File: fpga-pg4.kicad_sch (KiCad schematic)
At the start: 16 parts, among them U1 XC7A15T-FTG256

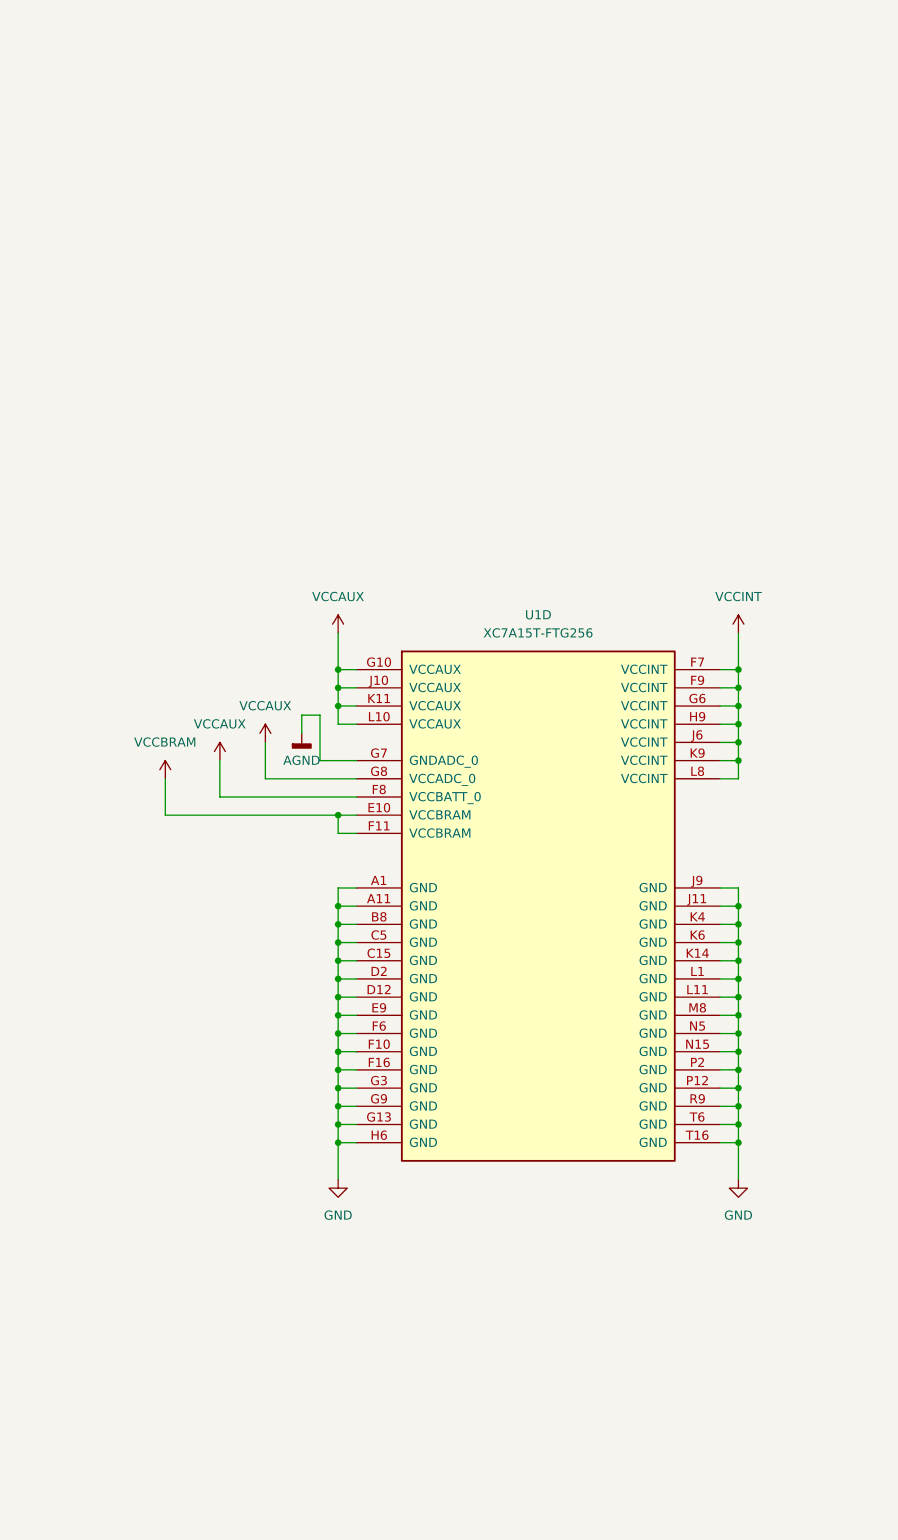
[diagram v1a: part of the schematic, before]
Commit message: changed ftg256 to csg325, wanted xc7a12t but couldnt find
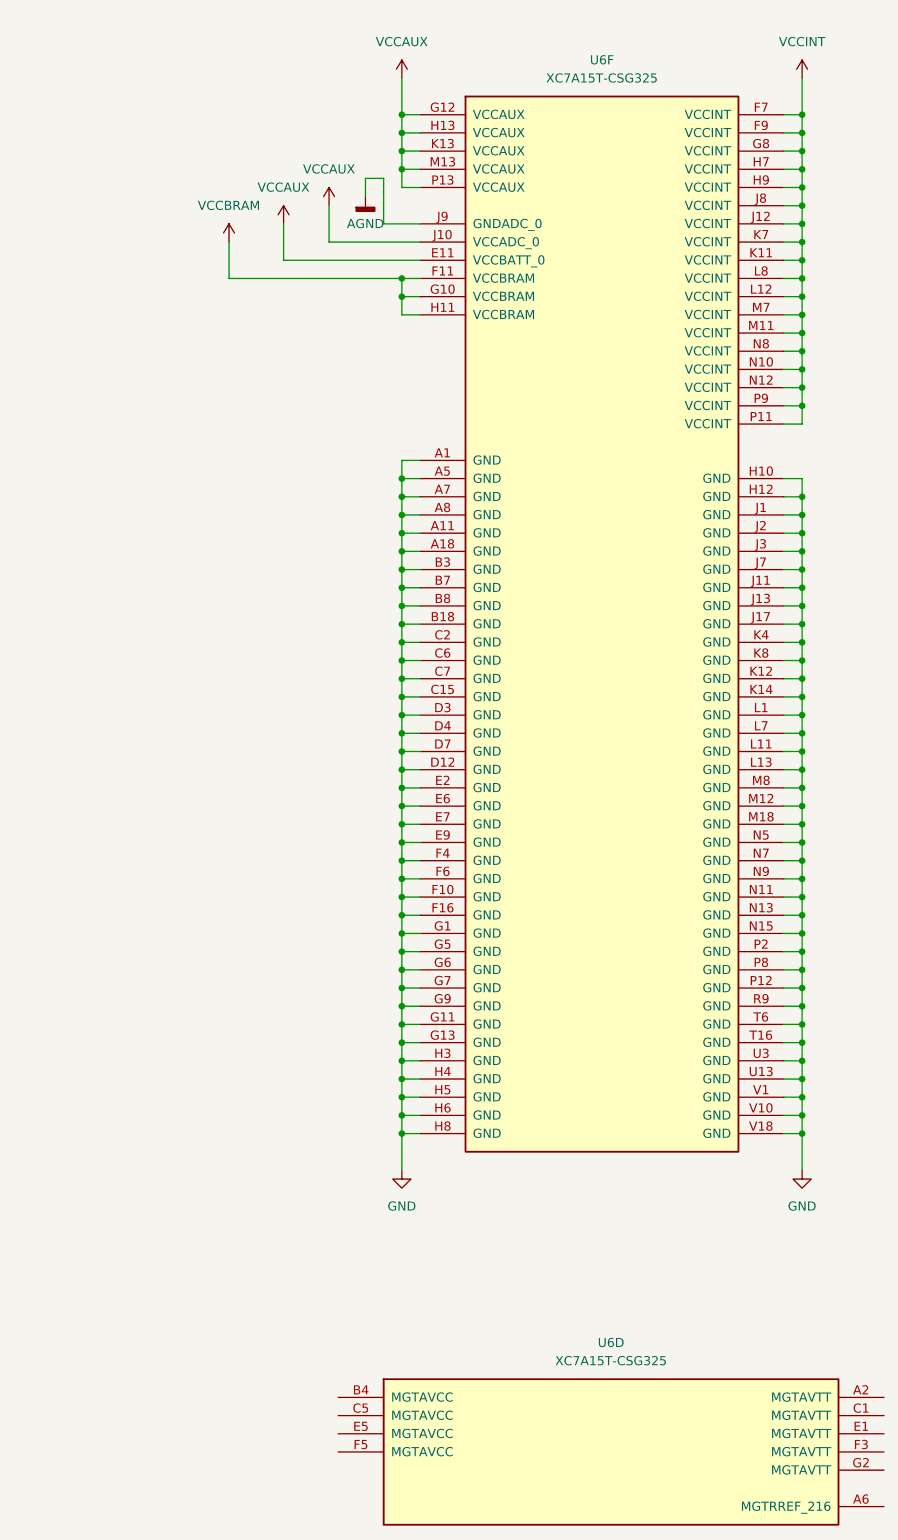
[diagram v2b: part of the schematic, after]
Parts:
- removed U1: XC7A15T-FTG256, Package_BGA:Xilinx_FTG256, symbol FPGA_Xilinx_Artix7:XC7A15T-FTG256
- added U6: XC7A15T-CSG325, Package_BGA:Xilinx_CSG325, symbol FPGA_Xilinx_Artix7:XC7A15T-CSG325
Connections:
- net AGND: now also U6.J9 (GNDADC_0)
- net GND: now also U6.A1 (GND), U6.A11 (GND), U6.A18 (GND), U6.A5 (GND), U6.A7 (GND), U6.A8 (GND), U6.B18 (GND), U6.B3 (GND), U6.B7 (GND), U6.B8 (GND), U6.C15 (GND), U6.C2 (GND), U6.C6 (GND), U6.C7 (GND), U6.D12 (GND), U6.D3 (GND), U6.D4 (GND), U6.D7 (GND), U6.E2 (GND), U6.E6 (GND), U6.E7 (GND), U6.E9 (GND), U6.F10 (GND), U6.F16 (GND), U6.F4 (GND), U6.F6 (GND), U6.G1 (GND), U6.G11 (GND), U6.G13 (GND), U6.G5 (GND), U6.G6 (GND), U6.G7 (GND), U6.G9 (GND), U6.H10 (GND), U6.H12 (GND), U6.H3 (GND), U6.H4 (GND), U6.H5 (GND), U6.H6 (GND), U6.H8 (GND), U6.J1 (GND), U6.J11 (GND), U6.J13 (GND), U6.J17 (GND), U6.J2 (GND), U6.J3 (GND), U6.J7 (GND), U6.K12 (GND), U6.K14 (GND), U6.K4 (GND), U6.K8 (GND), U6.L1 (GND), U6.L11 (GND), U6.L13 (GND), U6.L7 (GND), U6.M12 (GND), U6.M18 (GND), U6.M8 (GND), U6.N11 (GND), U6.N13 (GND), U6.N15 (GND), U6.N5 (GND), U6.N7 (GND), U6.N9 (GND), U6.P12 (GND), U6.P2 (GND), U6.P8 (GND), U6.R9 (GND), U6.T16 (GND), U6.T6 (GND), U6.U13 (GND), U6.U3 (GND), U6.V1 (GND), U6.V10 (GND), U6.V18 (GND)
- net VCCAUX: now also U6.E11 (VCCBATT_0), U6.G12 (VCCAUX), U6.H13 (VCCAUX), U6.J10 (VCCADC_0), U6.K13 (VCCAUX), U6.M13 (VCCAUX), U6.P13 (VCCAUX)
- net VCCBRAM: now also U6.F11 (VCCBRAM), U6.G10 (VCCBRAM), U6.H11 (VCCBRAM)
- net VCCINT: now also U6.F7 (VCCINT), U6.F9 (VCCINT), U6.G8 (VCCINT), U6.H7 (VCCINT), U6.H9 (VCCINT), U6.J12 (VCCINT), U6.J8 (VCCINT), U6.K11 (VCCINT), U6.K7 (VCCINT), U6.L12 (VCCINT), U6.L8 (VCCINT), U6.M11 (VCCINT), U6.M7 (VCCINT), U6.N10 (VCCINT), U6.N12 (VCCINT), U6.N8 (VCCINT), U6.P11 (VCCINT), U6.P9 (VCCINT)

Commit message: working on ddr3
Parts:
- removed unit 4 of U6
- added C30, C35: 4.7u, Capacitor_SMD:C_0805_2012Metric, symbol Device:C
- added C31, C32, C33, C34: 100n, Capacitor_SMD:C_0603_1608Metric, symbol Device:C
- added R17: 100, Capacitor_SMD:C_0402_1005Metric, symbol Device:R
- added U1: XC7A15T-CSG325, Package_BGA:Xilinx_CSG325, symbol FPGA_Xilinx_Artix7:XC7A15T-CSG325
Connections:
- net VCCINT is gone; now on net +V1P0: C10.1, C11.1, C12.1, C13.1, C9.1, U6.F7 (VCCINT), U6.F9 (VCCINT), U6.G8 (VCCINT), U6.H7 (VCCINT), U6.H9 (VCCINT), U6.J12 (VCCINT), U6.J8 (VCCINT), U6.K11 (VCCINT), U6.K7 (VCCINT), U6.L12 (VCCINT), U6.L8 (VCCINT), U6.M11 (VCCINT), U6.M7 (VCCINT), U6.N10 (VCCINT), U6.N12 (VCCINT), U6.N8 (VCCINT), U6.P11 (VCCINT), U6.P9 (VCCINT)
- net GND: now also C30.2, C31.2, C32.2, C33.2, C34.2, C35.2
- net VCCAUX renamed +V1P8
- net VCCBRAM renamed +V1P0
- net +V1P0: now also C30.1, C31.1, C32.1, U1.B4 (MGTAVCC), U1.C5 (MGTAVCC), U1.E5 (MGTAVCC), U1.F5 (MGTAVCC)
- new net: R17.2, U1.A6 (MGTRREF_216)
- new net +V1P2: C33.1, C34.1, C35.1, R17.1, U1.A2 (MGTAVTT), U1.C1 (MGTAVTT), U1.E1 (MGTAVTT), U1.F3 (MGTAVTT), U1.G2 (MGTAVTT)
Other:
- moved on the sheet: C1, C10, C11, C12, C13, C2, C3, C4, C5, C6, C7, C8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

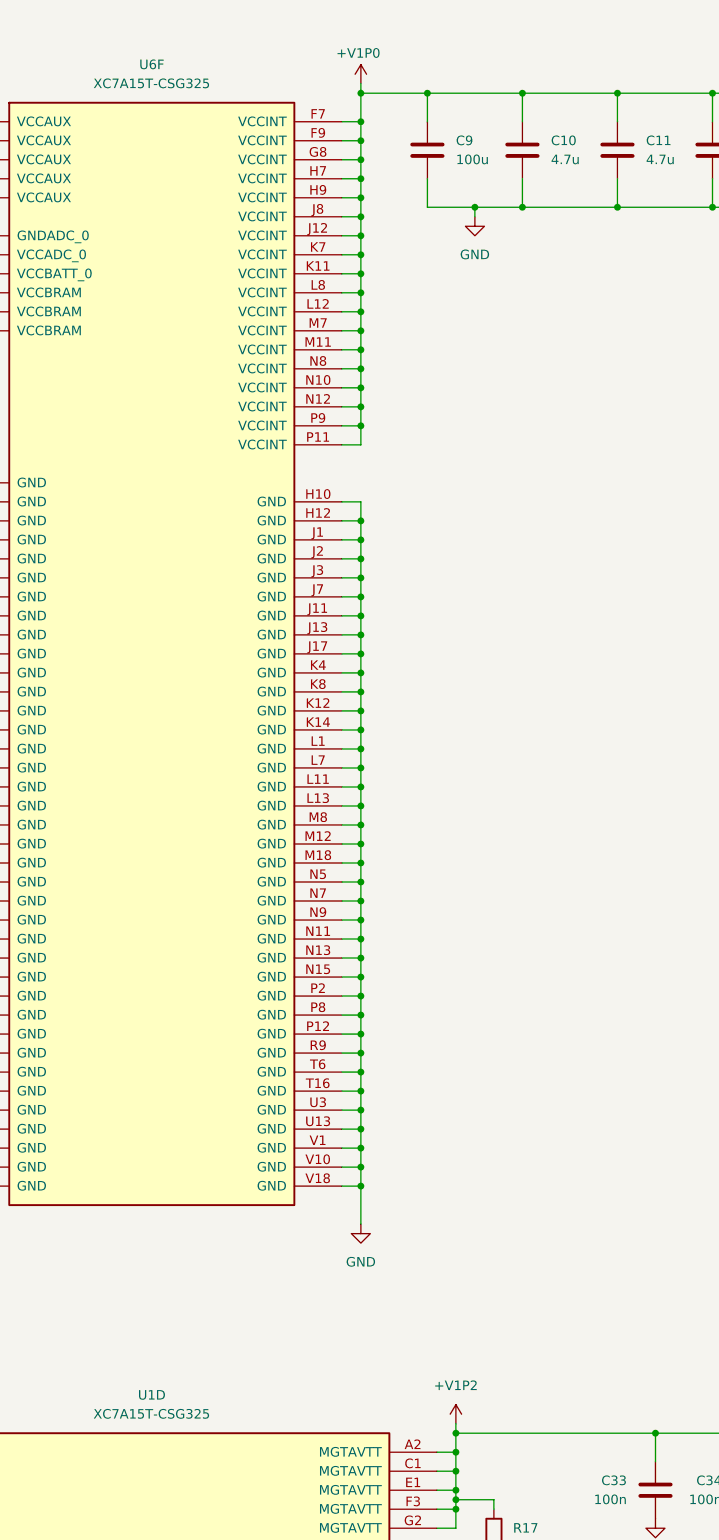
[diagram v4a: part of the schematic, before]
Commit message: placed decoupling caps for fpga
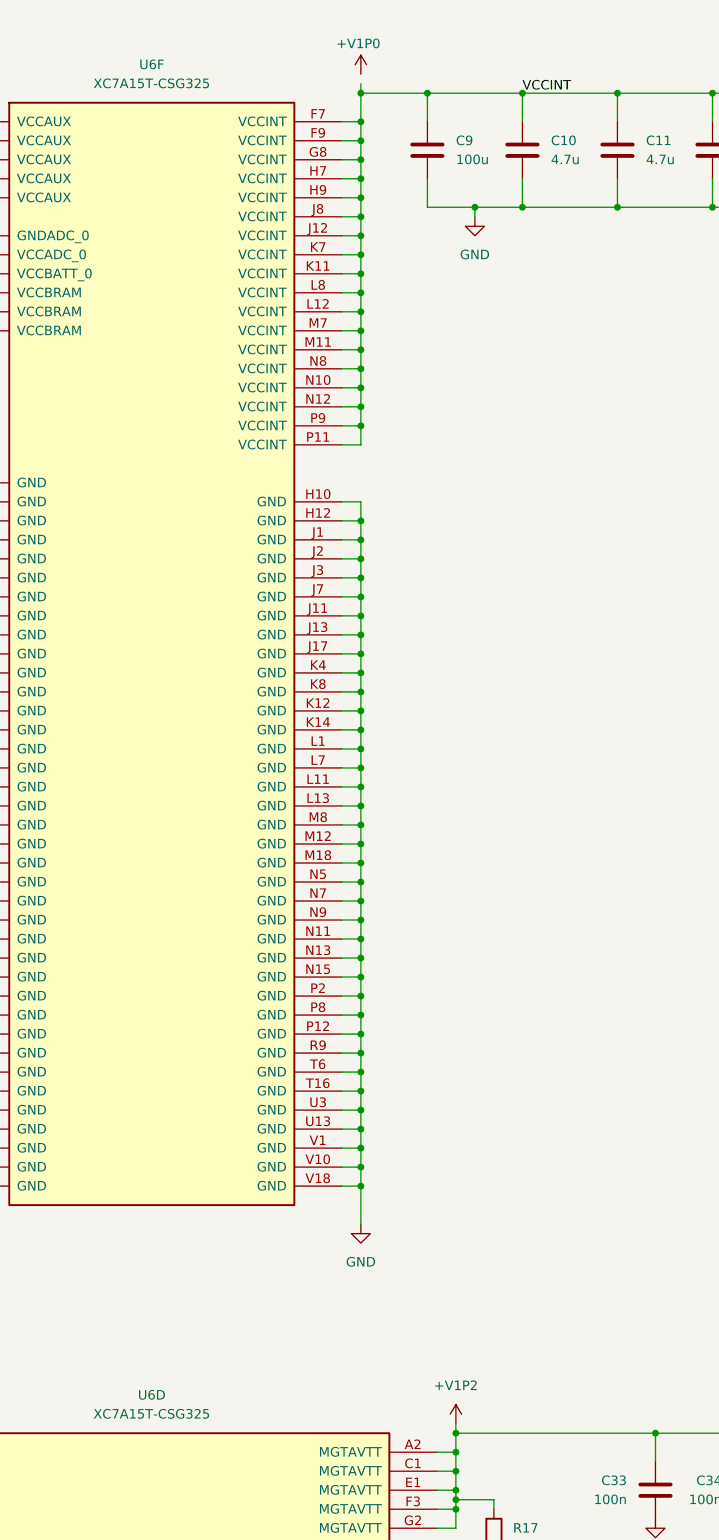
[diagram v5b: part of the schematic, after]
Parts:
- C1, C12, C13, C14, C15, C2, C3, C31, C32, C33, C34, C8: footprint Capacitor_SMD:C_0603_1608Metric -> Capacitor_SMD:C_0402_1005Metric
- C10, C11, C30, C35, C4, C5: footprint Capacitor_SMD:C_0805_2012Metric -> Capacitor_SMD:C_0402_1005Metric
- renumbered U1 to U6
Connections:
- net +V1P0: no longer C10.1, C11.1, C12.1, C13.1, C9.1, U6.F7 (VCCINT), U6.F9 (VCCINT), U6.G8 (VCCINT), U6.H7 (VCCINT), U6.H9 (VCCINT), U6.J12 (VCCINT), U6.J8 (VCCINT), U6.K11 (VCCINT), U6.K7 (VCCINT), U6.L12 (VCCINT), U6.L8 (VCCINT), U6.M11 (VCCINT), U6.M7 (VCCINT), U6.N10 (VCCINT), U6.N12 (VCCINT), U6.N8 (VCCINT), U6.P11 (VCCINT), U6.P9 (VCCINT)
- new net VCCINT: C10.1, C11.1, C12.1, C13.1, C9.1, U6.F7 (VCCINT), U6.F9 (VCCINT), U6.G8 (VCCINT), U6.H7 (VCCINT), U6.H9 (VCCINT), U6.J12 (VCCINT), U6.J8 (VCCINT), U6.K11 (VCCINT), U6.K7 (VCCINT), U6.L12 (VCCINT), U6.L8 (VCCINT), U6.M11 (VCCINT), U6.M7 (VCCINT), U6.N10 (VCCINT), U6.N12 (VCCINT), U6.N8 (VCCINT), U6.P11 (VCCINT), U6.P9 (VCCINT)
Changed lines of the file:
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@@
 		)
 	)
+	(label "VCCINT"
+		(at 276.86 35.56 0)
+		(effects
+			(font
+				(size 1.27 1.27)
+			)
+			(justify left bottom)
+		)
+	)
 	(symbol
 		(lib_id "power:VCC")
@@
 			)
 		)
-		(property "Footprint" "Capacitor_SMD:C_0805_2012Metric"
+		(property "Footprint" "Capacitor_SMD:C_0402_1005Metric"
 			(at 113.9952 46.99 0)
 			(effects
@@
 			)
 		)
-		(property "Footprint" "Capacitor_SMD:C_0805_2012Metric"
+		(property "Footprint" "Capacitor_SMD:C_0402_1005Metric"
 			(at 319.0748 226.06 0)
 			(effects
@@
 	(symbol
 		(lib_id "power:VCC")
-		(at 255.27 34.29 0)
+		(at 255.27 33.02 0)
 		(unit 1)
 		(exclude_from_sim no)
@@
 		(dnp no)
 		(property "Reference" "#PWR03"
-			(at 255.27 38.1 0)
+			(at 255.27 36.83 0)
 			(effects
 				(font
@@
 		)
 		(property "Value" "+V1P0"
-			(at 251.968 30.226 0)
+			(at 251.968 28.956 0)
 			(effects
 				(font
@@
 		)
 		(property "Footprint" ""
-			(at 255.27 34.29 0)
+			(at 255.27 33.02 0)
 			(effects
 				(font
@@
 		)
 		(property "Datasheet" ""
-			(at 255.27 34.29 0)
+			(at 255.27 33.02 0)
 			(effects
 				(font
@@
 		)
 		(property "Description" "Power symbol creates a global label with name \"VCC\""
-			(at 255.27 34.29 0)
+			(at 255.27 33.02 0)
 			(effects
 				(font
@@
 			)
 		)
-		(property "Footprint" "Capacitor_SMD:C_0805_2012Metric"
+		(property "Footprint" "Capacitor_SMD:C_0402_1005Metric"
 			(at 126.6952 46.99 0)
 			(effects
@@
 			)
 		)
-		(property "Footprint" "Capacitor_SMD:C_0603_1608Metric"
+		(property "Footprint" "Capacitor_SMD:C_0402_1005Metric"
 			(at 51.7652 162.56 0)
 			(effects
@@
 			)
 		)
-		(property "Footprint" "Capacitor_SMD:C_0603_1608Metric"
+		(property "Footprint" "Capacitor_SMD:C_0402_1005Metric"
 			(at 160.9852 226.06 0)
 			(effects
@@
 			)
 		)
-		(property "Footprint" "Capacitor_SMD:C_0603_1608Metric"
+		(property "Footprint" "Capacitor_SMD:C_0402_1005Metric"
 			(at 315.9252 46.99 0)
 			(effects
@@
 			)
 		)
-		(property "Footprint" "Capacitor_SMD:C_0603_1608Metric"
+		(property "Footprint" "Capacitor_SMD:C_0402_1005Metric"
 			(at 39.0652 162.56 0)
 			(effects
@@
 			)
 		)
-		(property "Footprint" "Capacitor_SMD:C_0805_2012Metric"
+		(property "Footprint" "Capacitor_SMD:C_0402_1005Metric"
 			(at 290.5252 46.99 0)
 			(effects
@@
 			)
 		)
-		(property "Footprint" "Capacitor_SMD:C_0603_1608Metric"
+		(property "Footprint" "Capacitor_SMD:C_0402_1005Metric"
 			(at 303.2252 46.99 0)
 			(effects
@@
 			)
 		)
-		(property "Footprint" "Capacitor_SMD:C_0603_1608Metric"
+		(property "Footprint" "Capacitor_SMD:C_0402_1005Metric"
 			(at 168.6052 73.66 0)
 			(effects
@@
 		(dnp no)
 		(fields_autoplaced yes)
-		(property "Reference" "U1"
+		(property "Reference" "U6"
 			(at 227.33 209.55 0)
 			(effects
@@
 			(project "logix-core"
 				(path "/cf3b7c5f-6ddc-4e3f-9529-0bcf5eec6f23/824409ff-e0aa-4944-ad80-228eadb659f9/0be3540d-0ef7-4890-b983-c7f7caf1a192"
-					(reference "U1")
+					(reference "U6")
 					(unit 4)
 				)
@@
 			)
 		)
-		(property "Footprint" "Capacitor_SMD:C_0603_1608Metric"
+		(property "Footprint" "Capacitor_SMD:C_0402_1005Metric"
 			(at 173.6852 226.06 0)
 			(effects
@@
 			)
 		)
-		(property "Footprint" "Capacitor_SMD:C_0603_1608Metric"
+		(property "Footprint" "Capacitor_SMD:C_0402_1005Metric"
 			(at 152.0952 46.99 0)
 			(effects
@@
 			)
 		)
-		(property "Footprint" "Capacitor_SMD:C_0603_1608Metric"
+		(property "Footprint" "Capacitor_SMD:C_0402_1005Metric"
 			(at 306.3748 226.06 0)
 			(effects
@@
 			)
 		)
-		(property "Footprint" "Capacitor_SMD:C_0805_2012Metric"
+		(property "Footprint" "Capacitor_SMD:C_0402_1005Metric"
 			(at 277.8252 46.99 0)
 			(effects
@@
 			)
 		)
-		(property "Footprint" "Capacitor_SMD:C_0805_2012Metric"
+		(property "Footprint" "Capacitor_SMD:C_0402_1005Metric"
 			(at 148.2852 226.06 0)
 			(effects
@@
 			)
 		)
-		(property "Footprint" "Capacitor_SMD:C_0603_1608Metric"
+		(property "Footprint" "Capacitor_SMD:C_0402_1005Metric"
 			(at 293.6748 226.06 0)
 			(effects
@@
 			)
 		)
-		(property "Footprint" "Capacitor_SMD:C_0603_1608Metric"
+		(property "Footprint" "Capacitor_SMD:C_0402_1005Metric"
 			(at 164.7952 46.99 0)
 			(effects
@@
 			)
 		)
-		(property "Footprint" "Capacitor_SMD:C_0603_1608Metric"
+		(property "Footprint" "Capacitor_SMD:C_0402_1005Metric"
 			(at 139.3952 46.99 0)
 			(effects
